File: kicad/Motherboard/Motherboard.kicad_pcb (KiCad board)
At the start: 2 copper layers, 75 parts, among them J1 USB_C_Receptacle_USB2.0, J10 Conn_01x08_Pin, J11 Conn_01x08_Pin, J12 Conn_01x08_Pin, J13 Conn_01x08_Pin, J14 Conn_01x08_Pin, J15 Conn_01x08_Pin, J16 Conn_01x08_Pin, J17 Conn_01x08_Pin, J5 Conn_01x02_Pin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

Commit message: random sh
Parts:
- moved C8 2.64 mm to (88.5, 87.9)
- moved C23 0.21 mm to (107.7, 129.3)
- moved C24 0.16 mm to (110.5, 129.2)
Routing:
- added copper zone on B.Cu, net GND
- added copper zone on F.Cu, net GND
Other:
- board outline added: 72.1 x 52 mm
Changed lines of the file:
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@@
 		(tags "capacitor handsolder")
 		(property "Reference" "C14"
-			(at 0 -1.68 90)
+			(at 0.0145 -4.222 90)
 			(layer "F.SilkS")
 			(effects
@@
 	(footprint "Capacitor_SMD:C_1210_3225Metric_Pad1.33x2.70mm_HandSolder"
 		(layer "F.Cu")
-		(at 85.8595 87.8165 -90)
+		(at 88.5 87.9125 -90)
 		(descr "Capacitor SMD 1210 (3225 Metric), square (rectangular) end terminal, IPC_7351 nominal with elongated pad for handsoldering. (Body size source: IPC-SM-782 page 76, https://www.pcb-3d.com/wordpress/wp-content/uploads/ipc-sm-782a_amendment_1_and_2.pdf), generated with kicad-footprint-generator")
 		(tags "capacitor handsolder")
@@
 	(footprint "Capacitor_SMD:C_0805_2012Metric_Pad1.18x1.45mm_HandSolder"
 		(layer "F.Cu")
-		(at 110.655 129.243 -90)
+		(at 110.5 129.243 -90)
 		(descr "Capacitor SMD 0805 (2012 Metric), square (rectangular) end terminal, IPC_7351 nominal with elongated pad for handsoldering. (Body size source: IPC-SM-782 page 76, https://www.pcb-3d.com/wordpress/wp-content/uploads/ipc-sm-782a_amendment_1_and_2.pdf, https://docs.google.com/spreadsheets/d/1BsfQQcO9C6DZCsRaXUlFlo91Tg2WpOkGARC1WS5S8t0/edit?usp=sharing), generated with kicad-footprint-generator")
 		(tags "capacitor handsolder")
@@
 			(at 0 1.68 90)
 			(layer "F.Fab")
+			(hide yes)
 			(effects
 				(font
@@
 	(footprint "Capacitor_SMD:C_0805_2012Metric_Pad1.18x1.45mm_HandSolder"
 		(layer "F.Cu")
-		(at 107.861 129.243 90)
+		(at 107.65 129.2625 90)
 		(descr "Capacitor SMD 0805 (2012 Metric), square (rectangular) end terminal, IPC_7351 nominal with elongated pad for handsoldering. (Body size source: IPC-SM-782 page 76, https://www.pcb-3d.com/wordpress/wp-content/uploads/ipc-sm-782a_amendment_1_and_2.pdf, https://docs.google.com/spreadsheets/d/1BsfQQcO9C6DZCsRaXUlFlo91Tg2WpOkGARC1WS5S8t0/edit?usp=sharing), generated with kicad-footprint-generator")
 		(tags "capacitor handsolder")
@@
 			(at 0 1.68 90)
 			(layer "F.Fab")
+			(hide yes)
 			(effects
 				(font
@@
 			)
 		)
+	)
+	(gr_line
+		(start 156.2 79.25)
+		(end 84.1 79.25)
+		(stroke
+			(width 0.05)
+			(type default)
+		)
+		(layer "Edge.Cuts")
+	)
+	(gr_line
+		(start 156.2 131.25)
+		(end 156.2 79.25)
+		(stroke
+			(width 0.05)
+			(type default)
+		)
+		(layer "Edge.Cuts")
+	)
+	(gr_line
+		(start 84.1 79.25)
+		(end 84.1 131.2)
+		(stroke
+			(width 0.05)
+			(type default)
+		)
+		(layer "Edge.Cuts")
+	)
+	(gr_line
+		(start 84.1 131.2)
+		(end 156.2 131.25)
+		(stroke
+			(width 0.05)
+			(type default)
+		)
+		(layer "Edge.Cuts")
+	)
+	(zone
+		(net 153)
+		(net_name "GND")
+		(layers "F&B.Cu")
+		(hatch edge 0.5)
+		(connect_pads
+			(clearance 0.2)
+		)
+		(min_thickness 0.2)
+		(filled_areas_thickness no)
+		(fill yes
+			(thermal_gap 0.5)
+			(thermal_bridge_width 0.5)
+		)
+		(polygon
+			(pts
+				(xy 84.1 79.25) (xy 84.1 131.2) (xy 156.2 131.25) (xy 156.2 79.25)
+			)
+		)

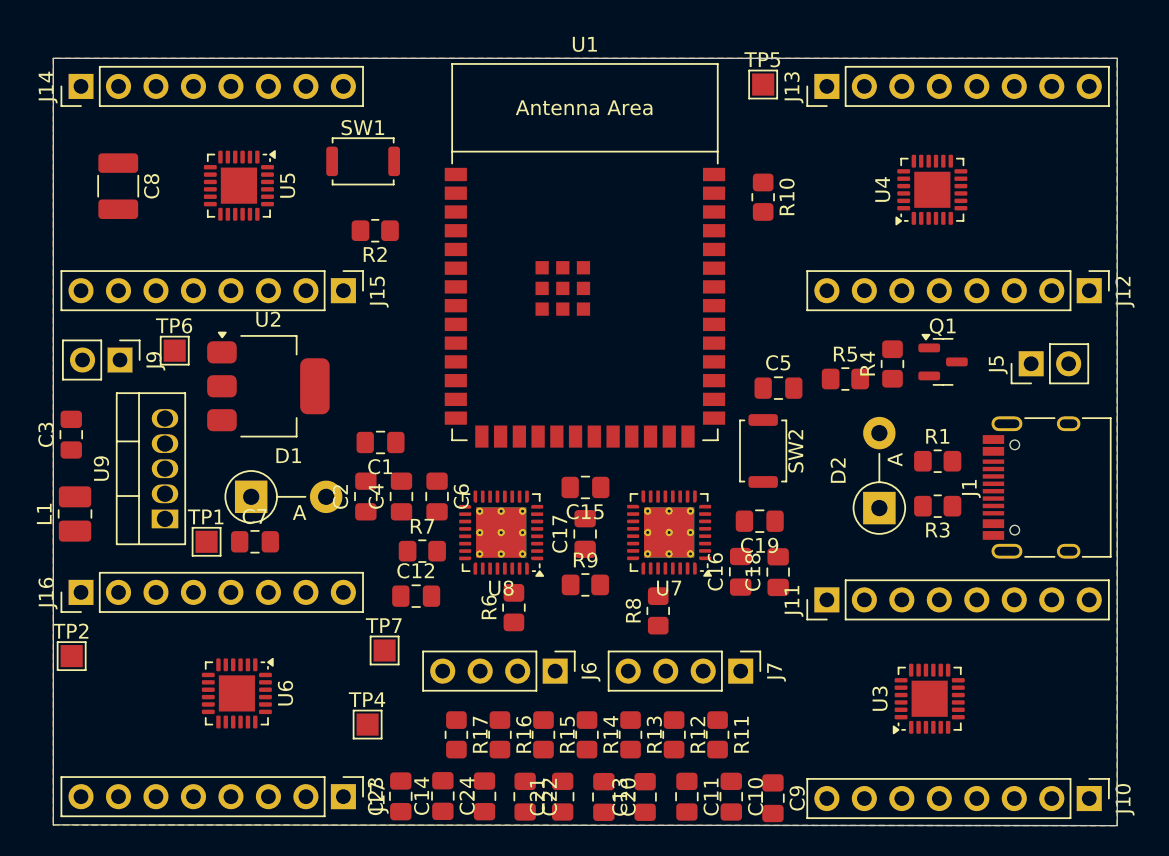
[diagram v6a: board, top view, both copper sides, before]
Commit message: schotty diode
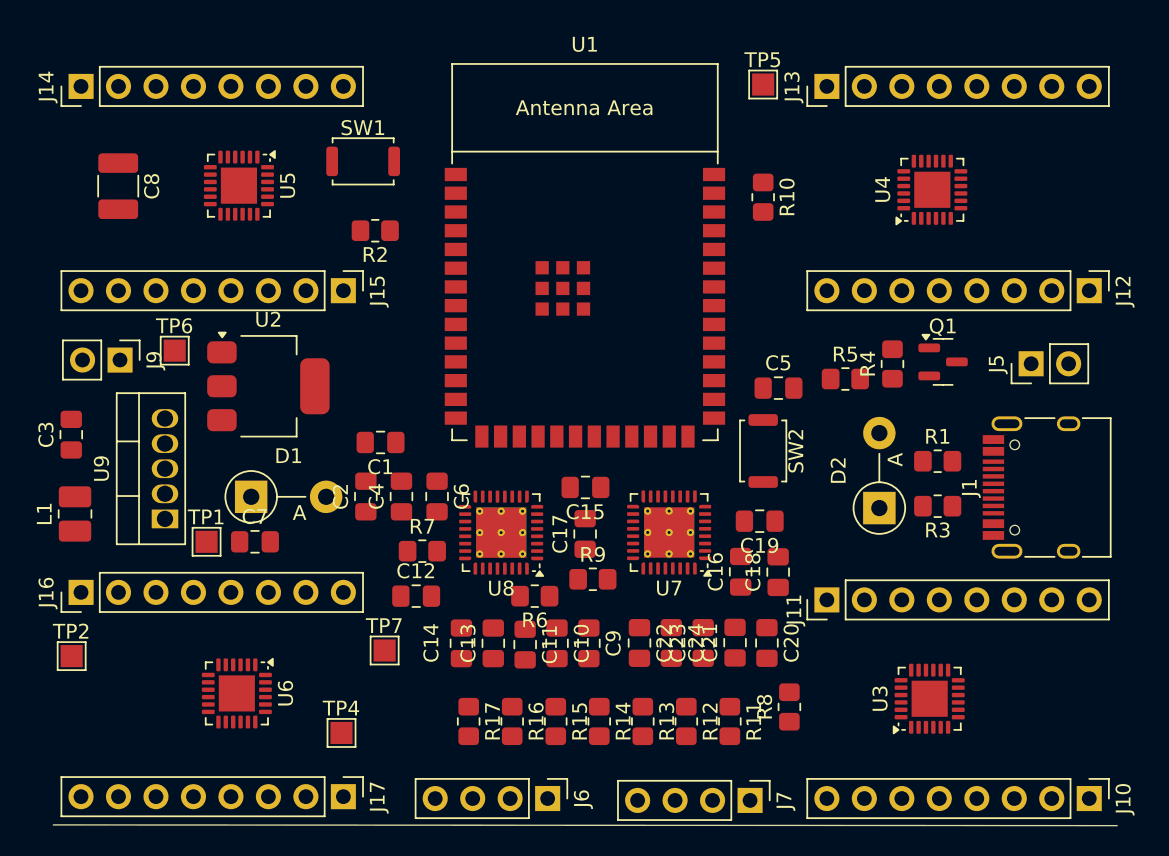
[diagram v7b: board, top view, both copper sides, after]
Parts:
- moved C23 23.0 mm to (128.1, 118.9)
- moved C24 18.6 mm to (126.0, 118.9)
- moved C9 16.3 mm to (120.4, 118.9)
- moved C10 15.7 mm to (118.2, 118.9)
- moved C21 15.7 mm to (130.3, 118.9)
- moved C20 15.2 mm to (132.5, 118.9)
- moved C11 15.0 mm to (116.1, 119.0)
- moved C13 14.6 mm to (113.9, 118.9)
- moved C22 13.0 mm to (123.8, 118.9)
- moved R8 11.0 mm to (134.0, 123.2)
- moved C14 10.5 mm to (111.8, 118.9)
- moved J7 8.79 mm to (131.3, 129.5)
- moved J6 8.65 mm to (117.6, 129.4)
- moved TP4 1.86 mm to (103.6, 125.0)
- moved R6 1.61 mm to (116.7, 115.7), turned to 180 degrees
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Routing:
- removed copper zone on B.Cu, net GND
- removed copper zone on F.Cu, net GND
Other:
- board size 72.1 x 52 mm -> 72.1 x 0.1 mm

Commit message: fixed layout
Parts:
- removed J14, J15, J16, J17: Conn_01x08_Pin, Connector_PinHeader_2.54mm:PinHeader_1x08_P2.54mm_Vertical
- removed R12, R13, R14, R15, R16, R17: 10k, Resistor_SMD:R_0805_2012Metric_Pad1.20x1.40mm_HandSolder
- removed TP6: TMC_Input1_TestPoint, TestPoint:TestPoint_Pad_1.5x1.5mm
- removed TP7: TMC_Input2_TestPoint, TestPoint:TestPoint_Pad_1.5x1.5mm
- added J2: Conn_01x02_Pin, Connector_PinHeader_2.54mm:PinHeader_1x02_P2.54mm_Vertical, F.Cu at (67.8, 78.0)
- added J3: Conn_01x04_Pin, Connector_PinHeader_2.54mm:PinHeader_1x04_P2.54mm_Vertical, F.Cu at (67.8, 65.8)
- added J4: Conn_01x04_Pin, Connector_PinHeader_2.54mm:PinHeader_1x04_P2.54mm_Vertical, F.Cu at (72.4, 65.8)
- added J8: Conn_01x08_Pin, Connector_PinHeader_2.54mm:PinHeader_1x08_P2.54mm_Vertical, F.Cu at (63.1, 65.8)
- added TP3: 3.3VConverter_TestPoint, TestPoint:TestPoint_Pad_1.5x1.5mm, F.Cu at (71.8, 77.5)
- J6, J7: value Conn_01x04_Pin -> Conn_01x08_Pin; footprint Connector_PinHeader_2.54mm:PinHeader_1x04_P2.54mm_Vertical -> Connector_PinHeader_2.54mm:PinHeader_1x08_P2.54mm_Vertical
- J9: value Conn_01x02_Pin -> Conn_01x08_Pin; footprint Connector_PinHeader_2.54mm:PinHeader_1x02_P2.54mm_Vertical -> Connector_PinHeader_2.54mm:PinHeader_1x08_P2.54mm_Vertical
- TP4: value AfterEM_TestPoint -> TMC_Input1_TestPoint
- TP5: value 3.3VConverter_TestPoint -> TMC_Input2_TestPoint
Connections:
- J5 pad 1: Net-(D2-A) -> Net-(J5-Pin_1)
- J5 pad 2: +5V -> GND
- J6 pad 1: Motor4_1 -> Net-(J6-Pin_1)
- J6 pad 2: Motor3_1 -> Net-(J6-Pin_2)
- J6 pad 3: Motor2_1 -> Net-(J6-Pin_3)
- J6 pad 4: Motor1_1 -> Net-(J6-Pin_4)
- J7 pad 1: Motor4_2 -> Net-(J7-Pin_1)
- J7 pad 2: Motor3_2 -> Net-(J7-Pin_2)
- J7 pad 3: Motor2_2 -> Net-(J7-Pin_3)
- J7 pad 4: Motor1_2 -> Net-(J7-Pin_4)
- J9 pad 1: VS_1 -> Net-(J9-Pin_1)
- J9 pad 2: GND -> Net-(J9-Pin_2)
- R11 pad 2: SCL -> SDA
- TP1 pad 1: VS_1 -> Net-(J5-Pin_1)
- TP4 pad 1: GND -> VS_1
- TP5 pad 1: +3.3V -> VS_1
- U3 pad 1: Net-(J10-Pin_8) -> Net-(J6-Pin_8)
- U3 pad 10: Net-(J11-Pin_8) -> Net-(J7-Pin_8)
- U3 pad 11: Net-(J11-Pin_7) -> Net-(J7-Pin_7)
- U3 pad 12: Net-(J11-Pin_6) -> Net-(J7-Pin_6)
- U3 pad 13: Net-(J11-Pin_5) -> Net-(J7-Pin_5)
- U3 pad 14: Net-(J11-Pin_4) -> Net-(J7-Pin_4)
- U3 pad 15: Net-(J11-Pin_3) -> Net-(J7-Pin_3)
- U3 pad 16: Net-(J11-Pin_2) -> Net-(J7-Pin_2)
- U3 pad 17: Net-(J11-Pin_1) -> Net-(J7-Pin_1)
- U3 pad 2: Net-(J10-Pin_7) -> Net-(J6-Pin_7)
- U3 pad 3: Net-(J10-Pin_6) -> Net-(J6-Pin_6)
- U3 pad 4: Net-(J10-Pin_5) -> Net-(J6-Pin_5)
- U3 pad 5: Net-(J10-Pin_4) -> Net-(J6-Pin_4)
- U3 pad 6: Net-(J10-Pin_3) -> Net-(J6-Pin_3)
- U3 pad 7: Net-(J10-Pin_2) -> Net-(J6-Pin_2)
- U3 pad 8: Net-(J10-Pin_1) -> Net-(J6-Pin_1)
- U4 pad 1: Net-(J12-Pin_8) -> Net-(J8-Pin_8)
- U4 pad 10: Net-(J13-Pin_8) -> Net-(J9-Pin_8)
- U4 pad 11: Net-(J13-Pin_7) -> Net-(J9-Pin_7)
- U4 pad 12: Net-(J13-Pin_6) -> Net-(J9-Pin_6)
- U4 pad 13: Net-(J13-Pin_5) -> Net-(J9-Pin_5)
- U4 pad 14: Net-(J13-Pin_4) -> Net-(J9-Pin_4)
- U4 pad 15: Net-(J13-Pin_3) -> Net-(J9-Pin_3)
- U4 pad 16: Net-(J13-Pin_2) -> Net-(J9-Pin_2)
- U4 pad 17: Net-(J13-Pin_1) -> Net-(J9-Pin_1)
- U4 pad 2: Net-(J12-Pin_7) -> Net-(J8-Pin_7)
- U4 pad 3: Net-(J12-Pin_6) -> Net-(J8-Pin_6)
- U4 pad 4: Net-(J12-Pin_5) -> Net-(J8-Pin_5)
- U4 pad 5: Net-(J12-Pin_4) -> Net-(J8-Pin_4)
- U4 pad 6: Net-(J12-Pin_3) -> Net-(J8-Pin_3)
- U4 pad 7: Net-(J12-Pin_2) -> Net-(J8-Pin_2)
- U4 pad 8: Net-(J12-Pin_1) -> Net-(J8-Pin_1)
- U5 pad 1: Net-(J14-Pin_8) -> Net-(J10-Pin_8)
- U5 pad 10: Net-(J15-Pin_8) -> Net-(J11-Pin_8)
- U5 pad 11: Net-(J15-Pin_7) -> Net-(J11-Pin_7)
- U5 pad 12: Net-(J15-Pin_6) -> Net-(J11-Pin_6)
- U5 pad 13: Net-(J15-Pin_5) -> Net-(J11-Pin_5)
- U5 pad 14: Net-(J15-Pin_4) -> Net-(J11-Pin_4)
- U5 pad 15: Net-(J15-Pin_3) -> Net-(J11-Pin_3)
- U5 pad 16: Net-(J15-Pin_2) -> Net-(J11-Pin_2)
- U5 pad 17: Net-(J15-Pin_1) -> Net-(J11-Pin_1)
- U5 pad 2: Net-(J14-Pin_7) -> Net-(J10-Pin_7)
- U5 pad 3: Net-(J14-Pin_6) -> Net-(J10-Pin_6)
- U5 pad 4: Net-(J14-Pin_5) -> Net-(J10-Pin_5)
- U5 pad 5: Net-(J14-Pin_4) -> Net-(J10-Pin_4)
- U5 pad 6: Net-(J14-Pin_3) -> Net-(J10-Pin_3)
- U5 pad 7: Net-(J14-Pin_2) -> Net-(J10-Pin_2)
- U5 pad 8: Net-(J14-Pin_1) -> Net-(J10-Pin_1)
- U6 pad 1: Net-(J16-Pin_8) -> Net-(J12-Pin_8)
- U6 pad 10: Net-(J17-Pin_8) -> Net-(J13-Pin_8)
- U6 pad 11: Net-(J17-Pin_7) -> Net-(J13-Pin_7)
- U6 pad 12: Net-(J17-Pin_6) -> Net-(J13-Pin_6)
- U6 pad 13: Net-(J17-Pin_5) -> Net-(J13-Pin_5)
- U6 pad 14: Net-(J17-Pin_4) -> Net-(J13-Pin_4)
- U6 pad 15: Net-(J17-Pin_3) -> Net-(J13-Pin_3)
- U6 pad 16: Net-(J17-Pin_2) -> Net-(J13-Pin_2)
- U6 pad 17: Net-(J17-Pin_1) -> Net-(J13-Pin_1)
- U6 pad 2: Net-(J16-Pin_7) -> Net-(J12-Pin_7)
- U6 pad 3: Net-(J16-Pin_6) -> Net-(J12-Pin_6)
- U6 pad 4: Net-(J16-Pin_5) -> Net-(J12-Pin_5)
- U6 pad 5: Net-(J16-Pin_4) -> Net-(J12-Pin_4)
- U6 pad 6: Net-(J16-Pin_3) -> Net-(J12-Pin_3)
- U6 pad 7: Net-(J16-Pin_2) -> Net-(J12-Pin_2)
- U6 pad 8: Net-(J16-Pin_1) -> Net-(J12-Pin_1)
